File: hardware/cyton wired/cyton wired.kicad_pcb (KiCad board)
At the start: 4 copper layers, 61.4 x 61.3 mm, 67 parts, among them J1 Conn_02x13_Odd_Even, J2 Conn_01x08, J3 Conn_01x04, J4 Conn_01x02, J5 Conn_01x04, U1 ADS129x, U2 CP2102N-Axx-xQFN24

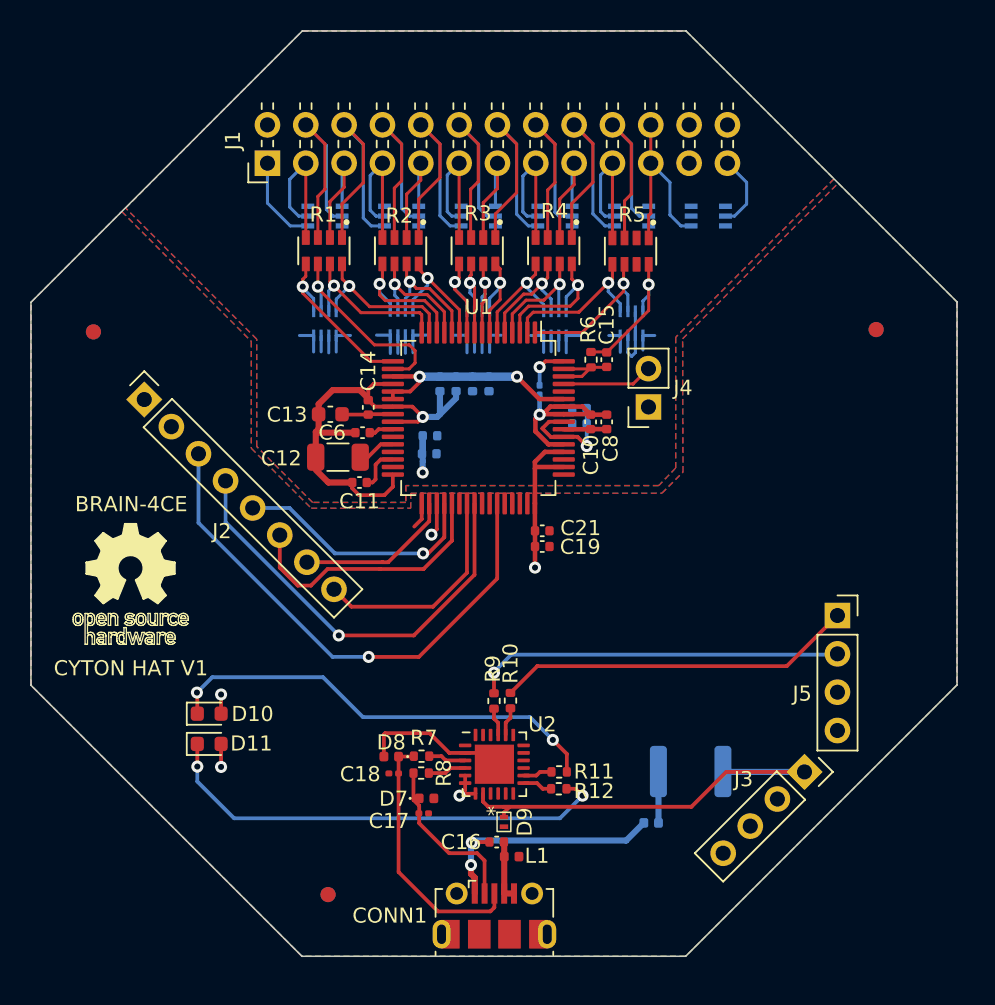
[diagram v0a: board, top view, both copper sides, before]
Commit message: added power supply
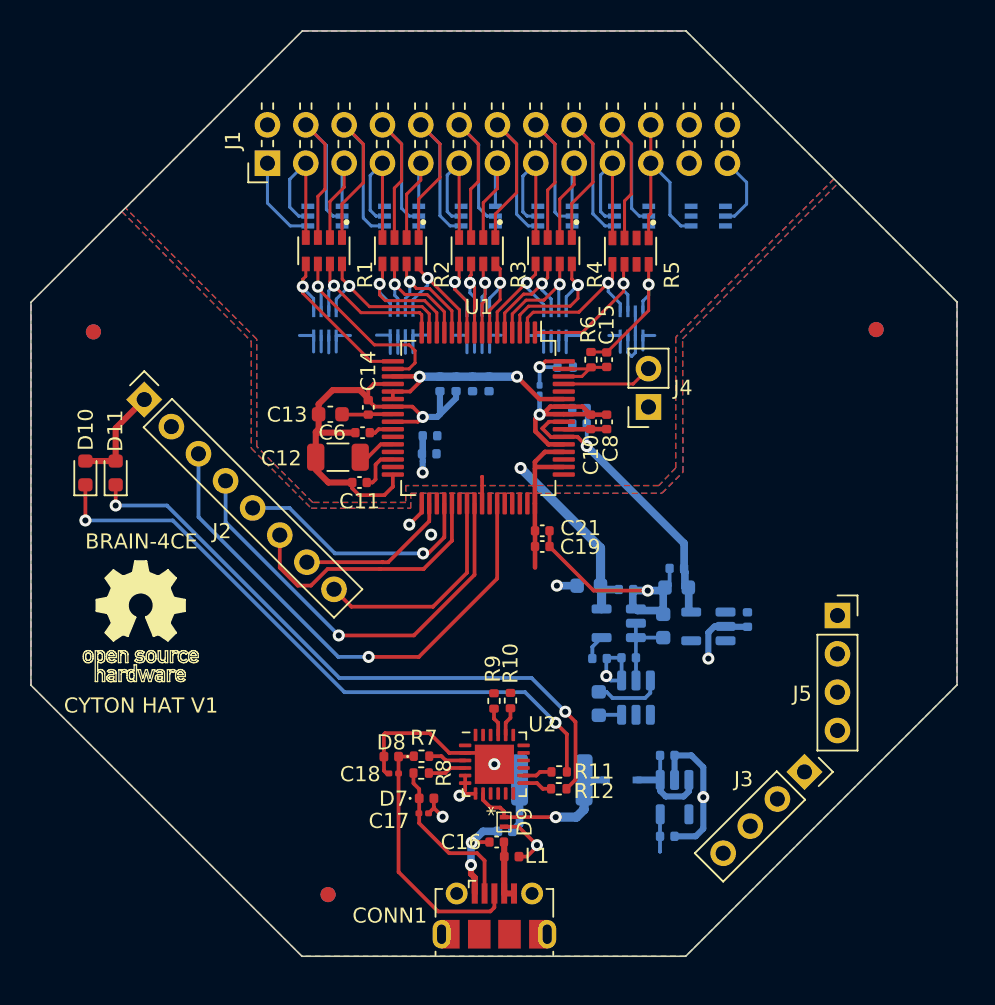
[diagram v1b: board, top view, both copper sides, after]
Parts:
- added C28: 2.2uF, Capacitor_SMD:C_0402_1005Metric, B.Cu at (151.2, 124.2)
- added C29: 10uF, Capacitor_SMD:C_0603_1608Metric, B.Cu at (146.6, 120.8)
- added C30: 10uF, Capacitor_SMD:C_0603_1608Metric, B.Cu at (150.9, 115.7)
- added C31: 2.2uF, Capacitor_SMD:C_0402_1005Metric, B.Cu at (151.2, 129.6)
- added C32: 2.2uF, Capacitor_SMD:C_0402_1005Metric, B.Cu at (156.5, 115.2)
- added C33: 2.2uF, Capacitor_SMD:C_0402_1005Metric, B.Cu at (148.6, 117.8)
- added C34: 0.01uF, Capacitor_SMD:C_0402_1005Metric, B.Cu at (146.7, 117.8)
- added C35: 2.2uF, Capacitor_SMD:C_0402_1005Metric, B.Cu at (151.8, 111.8)
- added C36: 10uF, Capacitor_SMD:C_0603_1608Metric, B.Cu at (151.8, 113.1)
- added C37: 2.2uF, Capacitor_SMD:C_0402_1005Metric, B.Cu at (148.4, 113.2)
- added C38: 10uF, Capacitor_SMD:C_0603_1608Metric, B.Cu at (146.0, 113.0)
- added D12: D_Zener, Diode_SMD:D_SOD-323, B.Cu at (148.1, 125.9)
- added R13: 0, Resistor_SMD:R_0402_1005Metric, B.Cu at (144.4, 98.5)
- added U3: MCP1754T-3302E/OT, Package_TO_SOT_SMD:SOT-23-5, B.Cu at (151.6, 127.0)
- added U4: LM2664, Package_TO_SOT_SMD:SOT-23-6, B.Cu at (149.1, 120.4)
- added U5: TPS7A24, Package_TO_SOT_SMD:SOT-23-5, B.Cu at (153.9, 115.7)
- added U6: TPS723xx-Q1, Package_TO_SOT_SMD:SOT-23-5, B.Cu at (147.9, 115.5)
- moved D11 19.0 mm to (114.6, 105.5), turned to 90 degrees
- moved D10 17.9 mm to (112.6, 105.5), turned to 90 degrees
- moved L2 9.69 mm to (140.4, 129.3)
- moved F1 9.22 mm to (143.5, 125.9)
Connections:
- J3 pad 1: VCOM -> unconnected-(J3-Pad1)
- J3 pad 3: VDD -> unconnected-(J3-Pad3)
- J3 pad 4: GNDA -> unconnected-(J3-Pad4)
- J5 pad 1: /RXD -> unconnected-(J5-Pad1)
- J5 pad 2: /TXD -> unconnected-(J5-Pad2)
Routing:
- net GNDA: track 44.8 -> 92.1 mm, vias 0 -> 9
- net /TXD: track 24.7 -> 0.00 mm, vias 1 -> 0
- net /RXD: track 23.8 -> 0.00 mm
- net VCOM: track 29.6 -> 11.4 mm, vias 0 -> 1
- net VDDA: track 27.3 -> 41.2 mm
- net Net-(D10-Pad1): track 29.6 -> 42.6 mm
- net VSSA: track 53.4 -> 66.2 mm, vias 3 -> 4
- net Net-(D11-Pad1): track 30.9 -> 42.6 mm
- net Net-(C16-Pad1): track 16.6 -> 6.91 mm
- net Net-(C28-Pad1): track 0.00 -> 6.83 mm
- net /Power Supply/-RAW: track 0.00 -> 5.60 mm
- net Net-(C29-Pad2): track 0.00 -> 4.55 mm
- net VDD: track 18.8 -> 23.1 mm, vias 5 -> 2
- net Net-(C34-Pad1): track 0.00 -> 1.64 mm
- net Net-(C29-Pad1): track 0.00 -> 1.53 mm
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- added copper zone on B.Cu, net VDD
- added copper zone on F.Cu, net VDD

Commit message: finished layout working on silkscreen
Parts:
- added C39: 18pF, Capacitor_SMD:C_0402_1005Metric, F.Cu at (145.0, 125.2)
- added C40: 18pF, Capacitor_SMD:C_0402_1005Metric, F.Cu at (144.5, 117.6)
- added C41: 10uF, Capacitor_SMD:C_0603_1608Metric, F.Cu at (127.7, 120.2)
- added D13: LED, LED_SMD:LED_0603_1608Metric, F.Cu at (129.8, 130.4)
- added R14: 1k, Resistor_SMD:R_0402_1005Metric, F.Cu at (127.2, 130.4)
- added R15: 470k, Resistor_SMD:R_0402_1005Metric, F.Cu at (155.1, 105.3)
- added R16: 470k, Resistor_SMD:R_0402_1005Metric, F.Cu at (153.0, 118.6)
- added SW1: SW_Push, Button_Switch_SMD:SW_SPST_PTS810, F.Cu at (154.5, 108.8)
- added SW2: SW_Push, Button_Switch_SMD:SW_SPST_PTS810, F.Cu at (154.5, 115.2)
- added U7: PIC32MX250F128B-I/SS, Package_SO:SSOP-28_5.3x10.2mm_P0.65mm, F.Cu at (134.0, 122.2)
- added Y1: ABMM2-8.000MHZ-E2-T, ABMM:XTAL_ABMM2-8.000MHZ-E2-T, F.Cu at (144.8, 121.4)
- C16, D9, L1: moved to B.Cu
- moved D10 40.6 mm to (150.0, 121.3), turned to 0 degrees
- moved D11 39.5 mm to (150.0, 122.9), turned to 0 degrees
- moved D8 17.7 mm to (147.0, 135.0), turned to -90 degrees
- moved C18 16.1 mm to (146.1, 134.8), turned to -90 degrees
- moved C17 15.8 mm to (150.0, 133.2), turned to 90 degrees
- moved R8 15.2 mm to (148.0, 133.0), turned to 90 degrees
- moved D7 15.1 mm to (149.0, 133.0), turned to 90 degrees
- moved R7 14.9 mm to (147.0, 133.0), turned to 90 degrees
- moved R9 9.00 mm to (143.3, 128.9), turned to 180 degrees
- moved U2 8.76 mm to (147.5, 128.8), turned to 90 degrees
- moved R10 7.60 mm to (143.3, 127.8), turned to 180 degrees
- moved D9 6.85 mm to (147.1, 127.6)
- moved R12 5.49 mm to (149.3, 124.9), turned to -90 degrees
- moved R11 4.26 mm to (148.2, 124.9), turned to -90 degrees
- moved C29 3.70 mm to (147.3, 117.2)
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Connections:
- net /_MISO renamed /MISO
- J3 pad 1: unconnected-(J3-Pad1) -> /D13
- J3 pad 2: unconnected-(J3-Pad2) -> /PGC
- J3 pad 3: unconnected-(J3-Pad3) -> VDD
- J3 pad 4: unconnected-(J3-Pad4) -> GNDA
- J5 pad 1: unconnected-(J5-Pad1) -> /BOOT_EN
- J5 pad 2: unconnected-(J5-Pad2) -> /MCLR
- J5 pad 3: unconnected-(J5-Pad3) -> /D18
- J5 pad 4: unconnected-(J5-Pad4) -> /PGD
- U1 pad 39: /CS2 -> /CS1
- U1 pad 47: /Daisy Functionality/_DRDY -> /DRDY
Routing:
- net Net-(D11-K): track 42.6 -> 1.57 mm, vias 2 -> 0
- net /PGD: track 0.00 -> 39.9 mm, vias 0 -> 2
- net Net-(D10-K): track 42.6 -> 3.71 mm, vias 2 -> 0
- net /BOOT_EN: track 0.00 -> 38.3 mm, vias 0 -> 1
- net /MCLR: track 0.00 -> 35.6 mm, vias 0 -> 2
- net VDD: track 23.1 -> 55.2 mm, vias 2 -> 10
- net /D18: track 0.00 -> 25.1 mm, vias 0 -> 1
- net /DRDY: track 0.00 -> 24.3 mm, vias 0 -> 2
- net /D13: track 0.00 -> 24.3 mm, vias 0 -> 1
- net /MISO: track 35.0 -> 59.2 mm
- net /PGC: track 0.00 -> 22.8 mm, vias 0 -> 1
- net /SCLK: track 28.7 -> 51.4 mm
- net /CS1: track 0.00 -> 21.6 mm, vias 0 -> 2
- net /MOSI: track 10.4 -> 30.3 mm, vias 0 -> 1
- net /RESET: track 16.6 -> 36.4 mm
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- removed copper zone on B.Cu, net VDD
- removed copper zone on F.Cu, net VDD

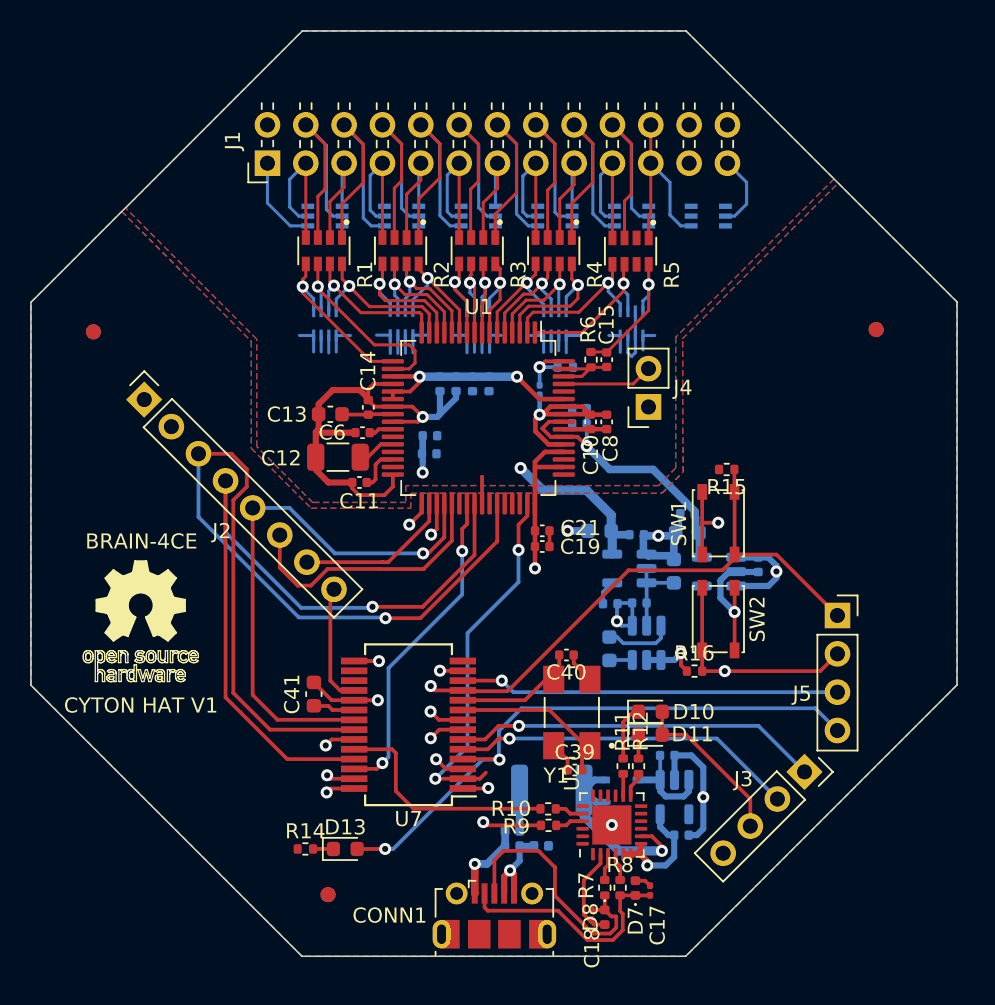
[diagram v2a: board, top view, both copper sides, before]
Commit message: fixed silk and generated fab outputs
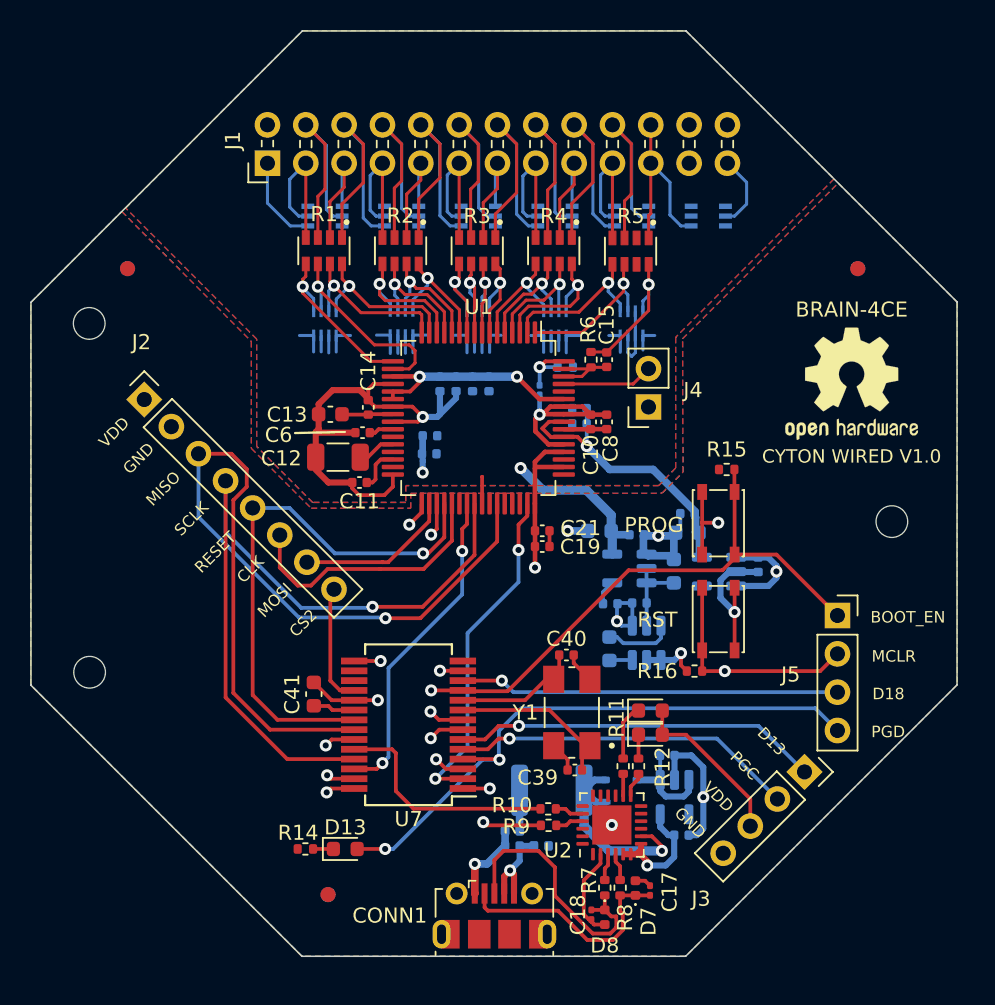
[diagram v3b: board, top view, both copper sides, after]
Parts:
- added ?: , , F.Cu at (112.9, 118.7)
- added ?: , , F.Cu at (112.9, 95.6)
- added REF**: MountingHole_2.1mm, MountingHole:MountingHole_2.1mm, F.Cu at (166.0, 108.7)
- added REF**: OSHW-Logo2_9.8x8mm_SilkScreen, Symbol:OSHW-Logo2_9.8x8mm_SilkScreen, F.Cu at (163.4, 99.6)
- added REF**: KiCad-Logo2_5mm_SilkScreen, Symbol:KiCad-Logo2_5mm_SilkScreen, B.Cu at (163.4, 102.5)
- D1, D2, D3, D4, D5, D6: value TPD4E1B06DCKR -> DCK6_TEX
- moved REF** 4.76 mm to (115.4, 92.0) (x2)
- moved REF** 4.22 mm to (163.8, 92.0) (x2)
- moved D10 0.08 mm to (150.0, 121.3)
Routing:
- net /DRDY: track 24.3 -> 22.6 mm
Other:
- board text added: "BOOT_EN"
- board text added: "CLK"
- board text added: "CS2"
- board text added: "CYTON WIRED V1.0"
- board text added: "D13"
- board text added: "D18"
- board text added: "GND"
- board text added: "MCLR"
- board text added: "MISO"
- board text added: "MOSI"
- board text added: "PGC"
- board text added: "PGD"
- board text added: "PROG"
- board text added: "RESET"
- board text added: "RST"
- board text added: "SCLK"
- board text added: "VDD"
- board text removed: "CYTON HAT V1"

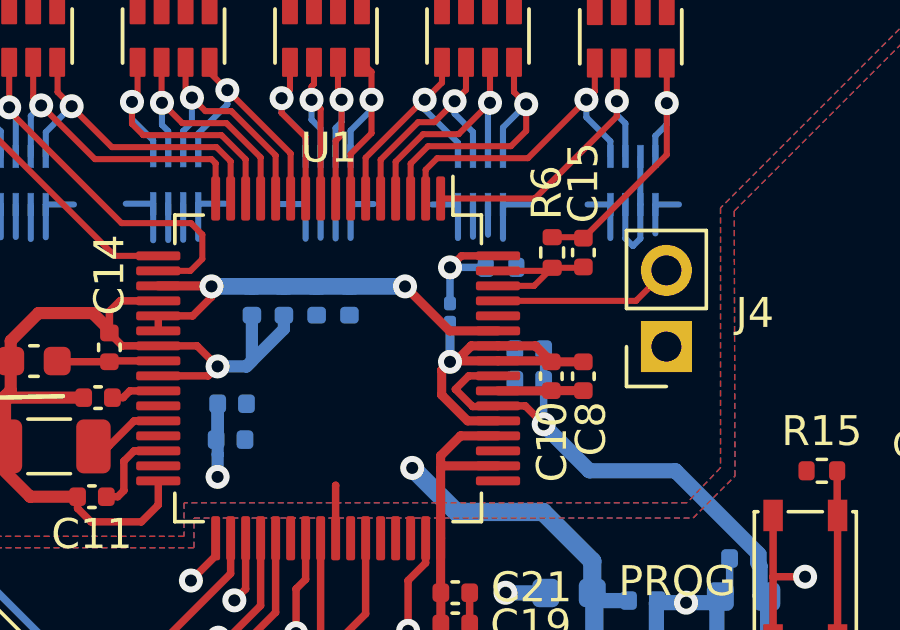
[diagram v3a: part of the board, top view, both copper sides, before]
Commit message: changed C27 from an 0402 package to a 0201 package
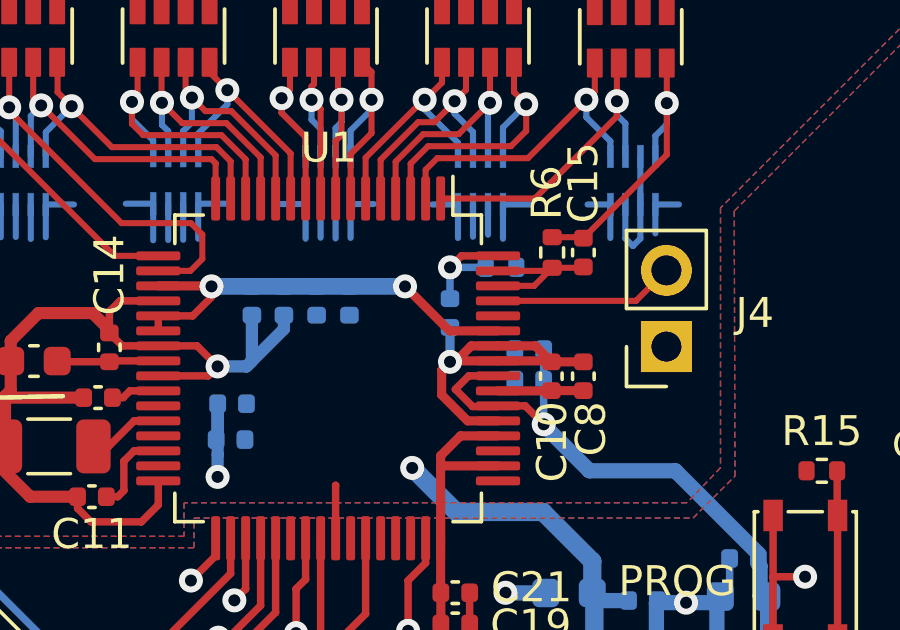
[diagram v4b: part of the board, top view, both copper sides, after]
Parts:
- C27: footprint Capacitor_SMD:C_0201_0603Metric -> Capacitor_SMD:C_0402_1005Metric
- D1, D2, D3, D4, D5, D6: value DCK6_TEX -> TPD4E1B06DCKR

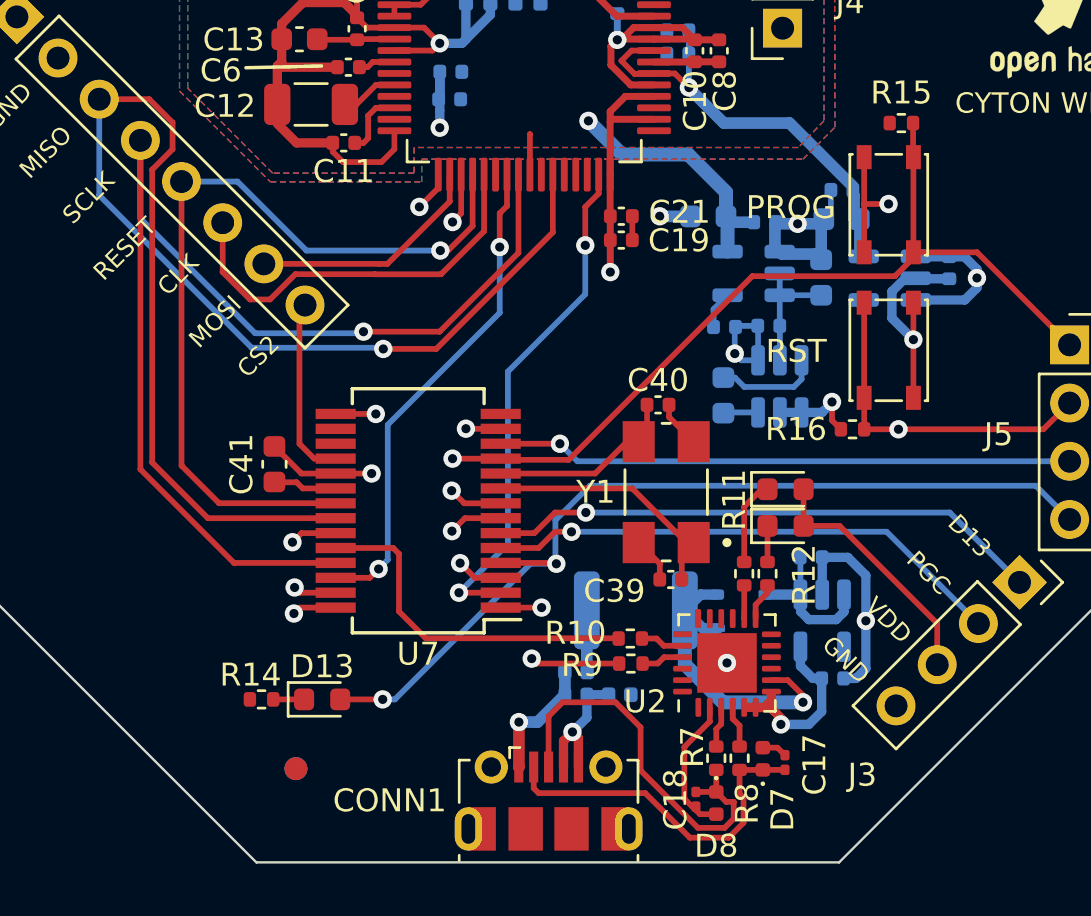
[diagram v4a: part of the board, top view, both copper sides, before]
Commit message: changed C27 from an 0402 package to a 0201 package
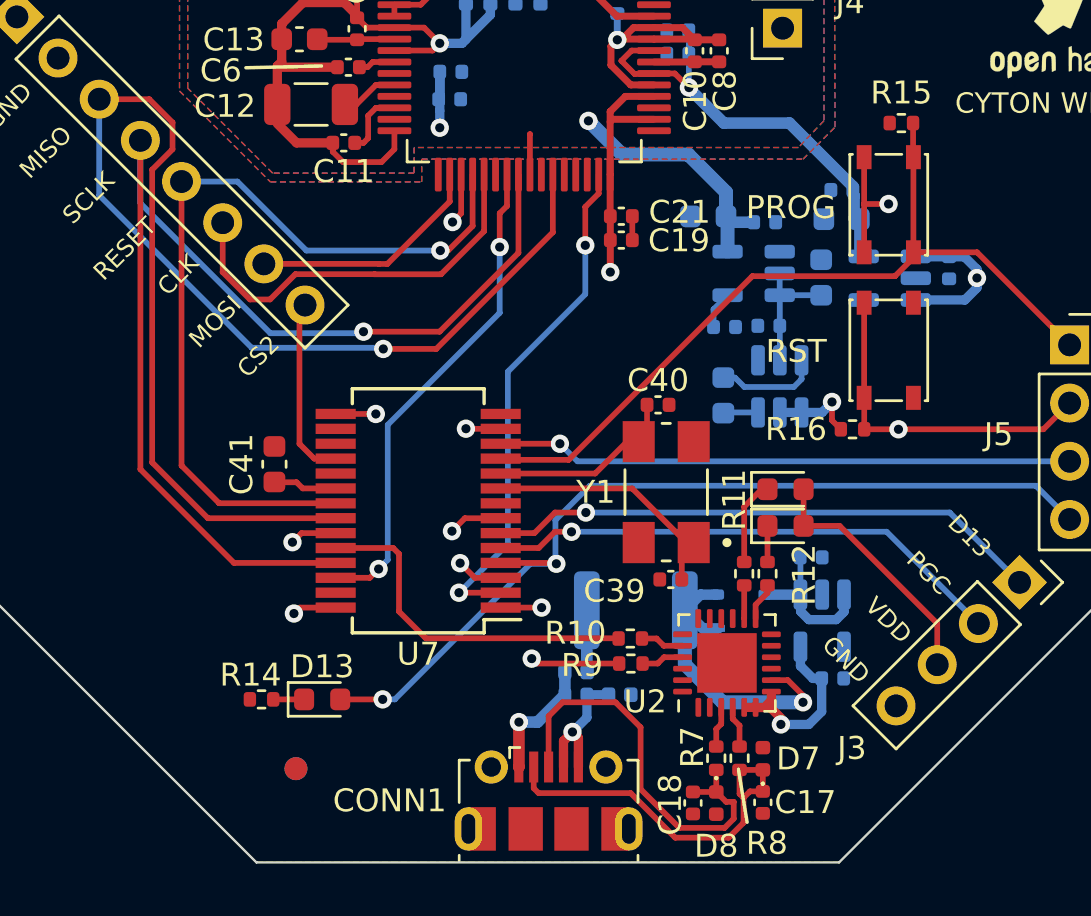
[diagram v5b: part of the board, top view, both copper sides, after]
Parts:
- C17, C18: footprint Capacitor_SMD:C_0201_0603Metric -> Capacitor_SMD:C_0402_1005Metric
- moved C17 1.99 mm to (149.0, 134.9), turned to -90 degrees
- moved C18 0.20 mm to (146.0, 134.9)
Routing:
- net GNDA: track 93.3 -> 37.3 mm, vias 10 -> 0
- net /BOOT_EN: track 38.2 -> 36.1 mm, vias 1 -> 0
- net Net-(CONN1-D-): track 15.6 -> 16.5 mm
- net Net-(CONN1-D+): track 17.6 -> 18.2 mm
